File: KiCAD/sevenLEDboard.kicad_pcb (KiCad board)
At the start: 2 copper layers, 23.1 x 20 mm, 13 parts, among them J1 Conn_01x03_Male, U1 ZXLD1350

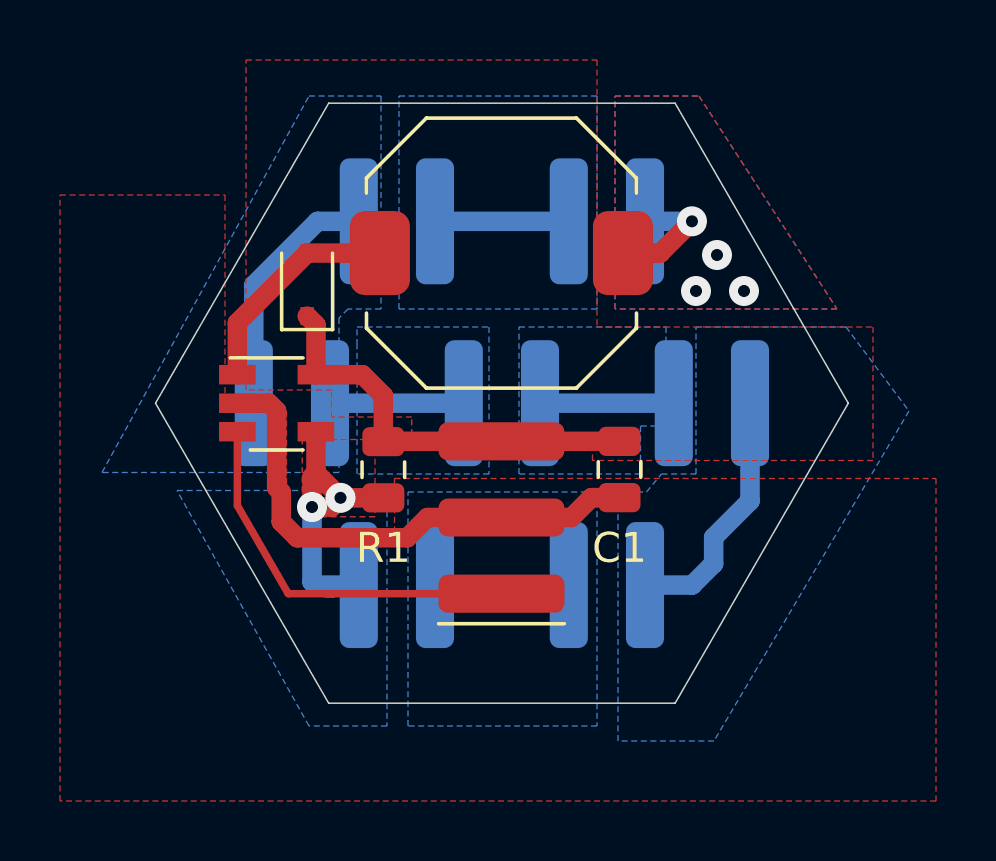
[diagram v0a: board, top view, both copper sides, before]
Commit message: Modified bracket and added stand.
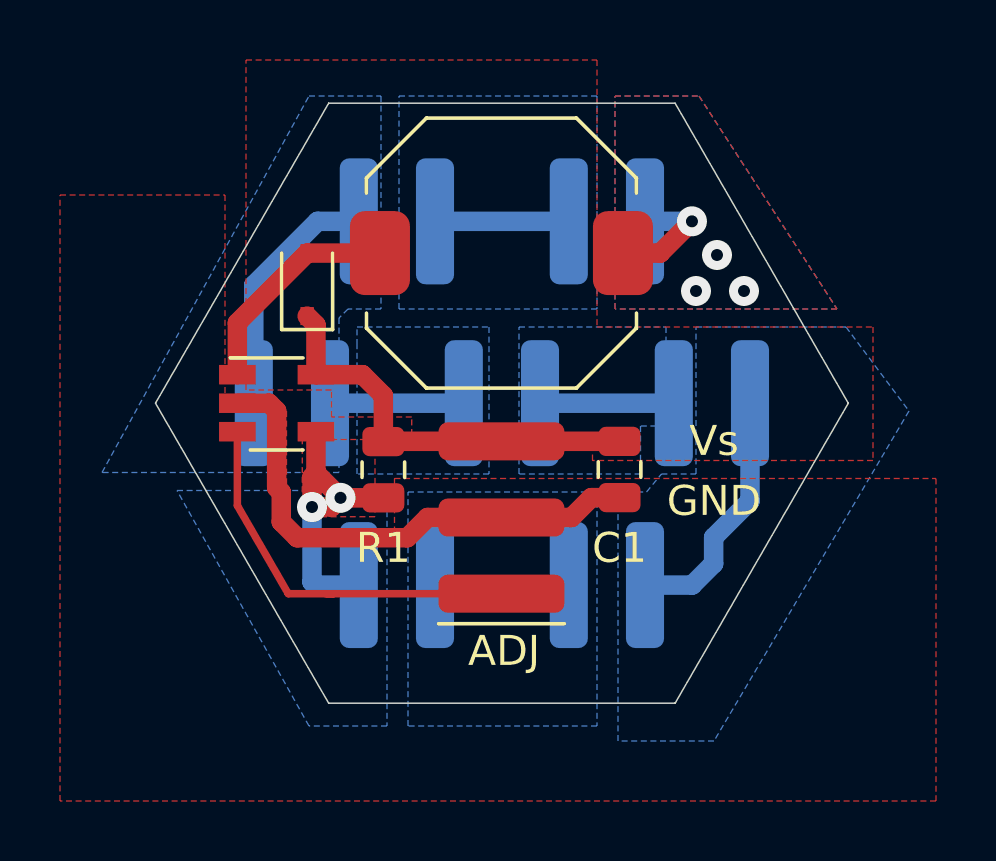
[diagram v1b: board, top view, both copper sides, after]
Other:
- board text added: "ADJ"
- board text added: "GND"
- board text added: "Vs"
